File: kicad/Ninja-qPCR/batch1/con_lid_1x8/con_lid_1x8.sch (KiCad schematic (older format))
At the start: 8 parts, among them T1 Conn_01x02_Male, T2 Conn_01x02_Male, T3 Conn_01x02_Male, T4 Conn_01x02_Male, U1 Conn_02x05

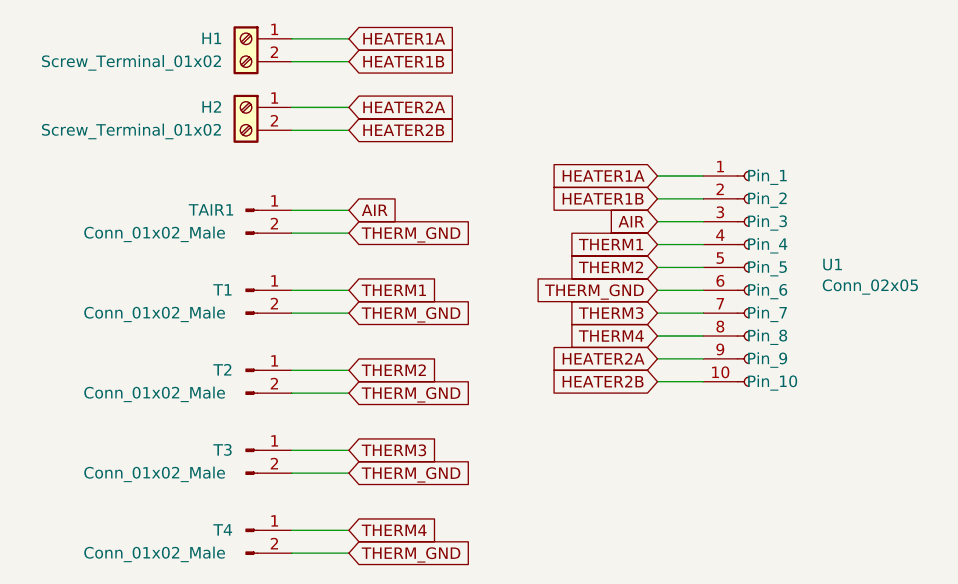
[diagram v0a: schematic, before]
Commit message: add schematics of test boards
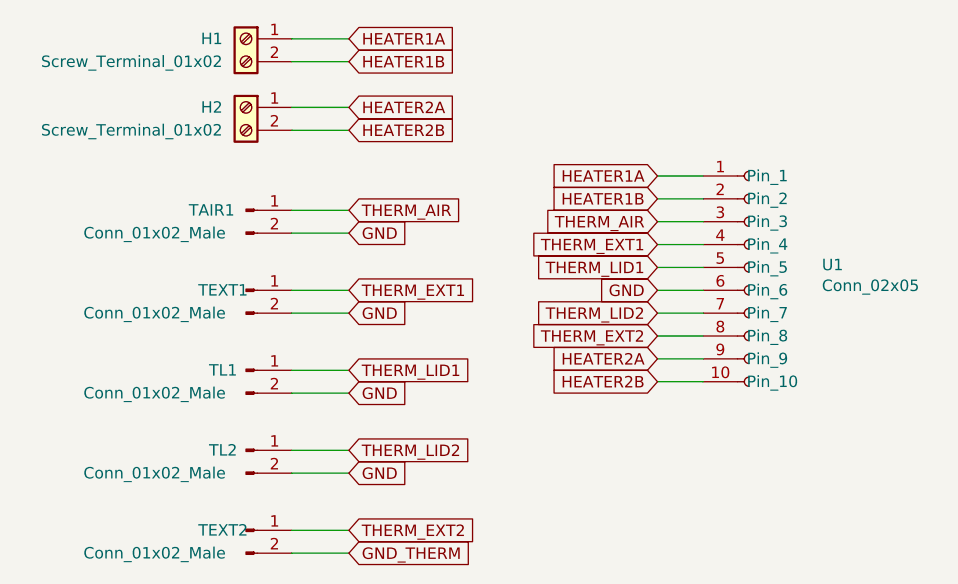
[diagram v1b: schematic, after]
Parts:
- renumbered T1 to TEXT1, T4 to TEXT2, T2 to TL1, T3 to TL2
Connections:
- net AIR renamed THERM_AIR
- net THERM1 renamed THERM_EXT1
- net THERM2 renamed THERM_LID1
- net THERM3 renamed THERM_LID2
- net THERM4 renamed THERM_EXT2
- net THERM_GND renamed GND
- net GND: no longer TEXT2.2 (Pin_2)
- new net GND_THERM: TEXT2.2 (Pin_2)
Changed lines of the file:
@@
 $EndComp
 $Comp
-L Connector:Conn_01x02_Male T1
+L Connector:Conn_01x02_Male TEXT1
 U 1 1 5F2B7778
 P 3300 3900
-F 0 "T1" H 3200 3900 50  0000 C CNN
+F 0 "TEXT1" H 3200 3900 50  0000 C CNN
 F 1 "Conn_01x02_Male" H 2900 3800 50  0000 C CNN
 F 2 "Pin_Headers:Pin_Header_Angled_1x02_Pitch2.54mm" H 3300 3900 50  0001 C CNN
@@
 $EndComp
 $Comp
-L Connector:Conn_01x02_Male T2
+L Connector:Conn_01x02_Male TL1
 U 1 1 5F2BA46F
 P 3300 4250
-F 0 "T2" H 3200 4250 50  0000 C CNN
+F 0 "TL1" H 3200 4250 50  0000 C CNN
 F 1 "Conn_01x02_Male" H 2900 4150 50  0000 C CNN
 F 2 "Pin_Headers:Pin_Header_Angled_1x02_Pitch2.54mm" H 3300 4250 50  0001 C CNN
@@
 $EndComp
 $Comp
-L Connector:Conn_01x02_Male T3
+L Connector:Conn_01x02_Male TL2
 U 1 1 5F2BA479
 P 3300 4600
-F 0 "T3" H 3200 4600 50  0000 C CNN
+F 0 "TL2" H 3200 4600 50  0000 C CNN
 F 1 "Conn_01x02_Male" H 2900 4500 50  0000 C CNN
 F 2 "Pin_Headers:Pin_Header_Angled_1x02_Pitch2.54mm" H 3300 4600 50  0001 C CNN
@@
 $EndComp
 $Comp
-L Connector:Conn_01x02_Male T4
+L Connector:Conn_01x02_Male TEXT2
 U 1 1 5F2BC0F4
 P 3300 4950
-F 0 "T4" H 3200 4950 50  0000 C CNN
+F 0 "TEXT2" H 3200 4950 50  0000 C CNN
 F 1 "Conn_01x02_Male" H 2900 4850 50  0000 C CNN
 F 2 "Pin_Headers:Pin_Header_Angled_1x02_Pitch2.54mm" H 3300 4950 50  0001 C CNN
@@
 HEATER2B
 Text GLabel 3750 3900 2    50   Input ~ 0
-THERM1
+THERM_EXT1
 Text GLabel 3750 4250 2    50   Input ~ 0
-THERM2
+THERM_LID1
 Text GLabel 3750 3550 2    50   Input ~ 0
-AIR
+THERM_AIR
 Text GLabel 3750 4600 2    50   Input ~ 0
-THERM3
+THERM_LID2
 Text GLabel 3750 4950 2    50   Input ~ 0
-THERM4
+THERM_EXT2
 Text GLabel 3750 5050 2    50   Input ~ 0
-THERM_GND
+GND_THERM
 Wire Wire Line
 	3500 3550 3750 3550
@@
 	3750 5050 3500 5050
 Text GLabel 3750 4700 2    50   Input ~ 0
-THERM_GND
+GND
 Text GLabel 3750 4350 2    50   Input ~ 0
-THERM_GND
+GND
 Text GLabel 3750 4000 2    50   Input ~ 0
-THERM_GND
+GND
 Text GLabel 3750 3650 2    50   Input ~ 0
-THERM_GND
+GND
 Wire Wire Line
 	3500 3650 3750 3650
@@
 HEATER2B
 Text GLabel 5100 3900 0    50   Input ~ 0
-THERM_GND
+GND
 Text GLabel 5100 3600 0    50   Input ~ 0
-AIR
+THERM_AIR
 Text GLabel 5100 3700 0    50   Input ~ 0
-THERM1
+THERM_EXT1
 Text GLabel 5100 3800 0    50   Input ~ 0
-THERM2
+THERM_LID1
 Text GLabel 5100 4000 0    50   Input ~ 0
-THERM3
+THERM_LID2
 Text GLabel 5100 4100 0    50   Input ~ 0
-THERM4
+THERM_EXT2
 Wire Wire Line
 	5100 3400 5300 3400
